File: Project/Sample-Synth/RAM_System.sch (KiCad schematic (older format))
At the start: 1 part

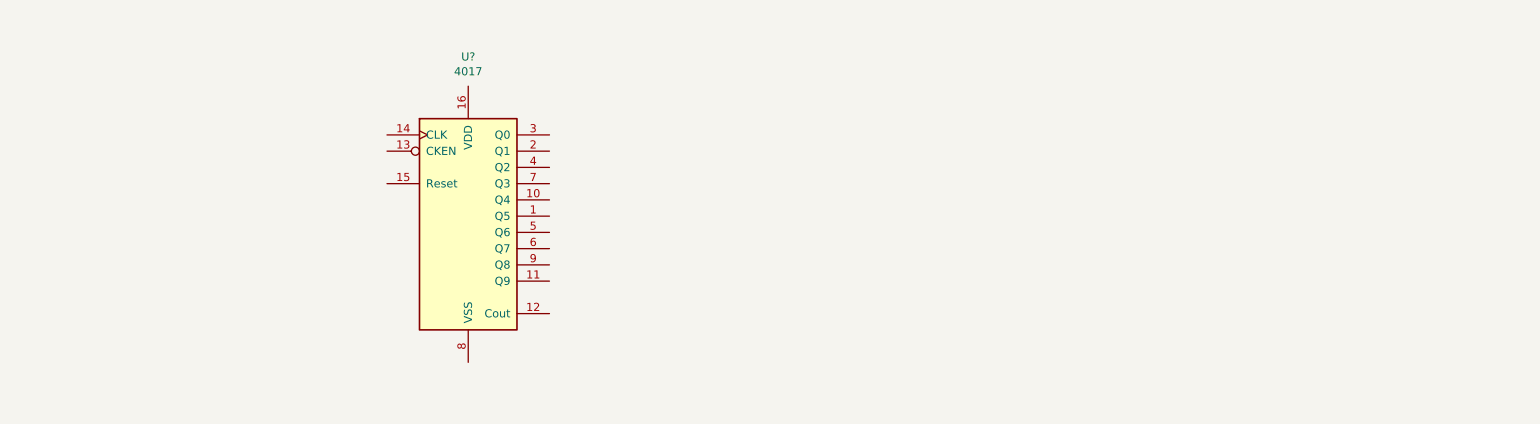
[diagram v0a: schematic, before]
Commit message: Updates to Schematic
Schematic updates: fixed connections on RAM, started setup for DAC stage.
Also swapped out the datasheet for the RAM to a more accurate one.
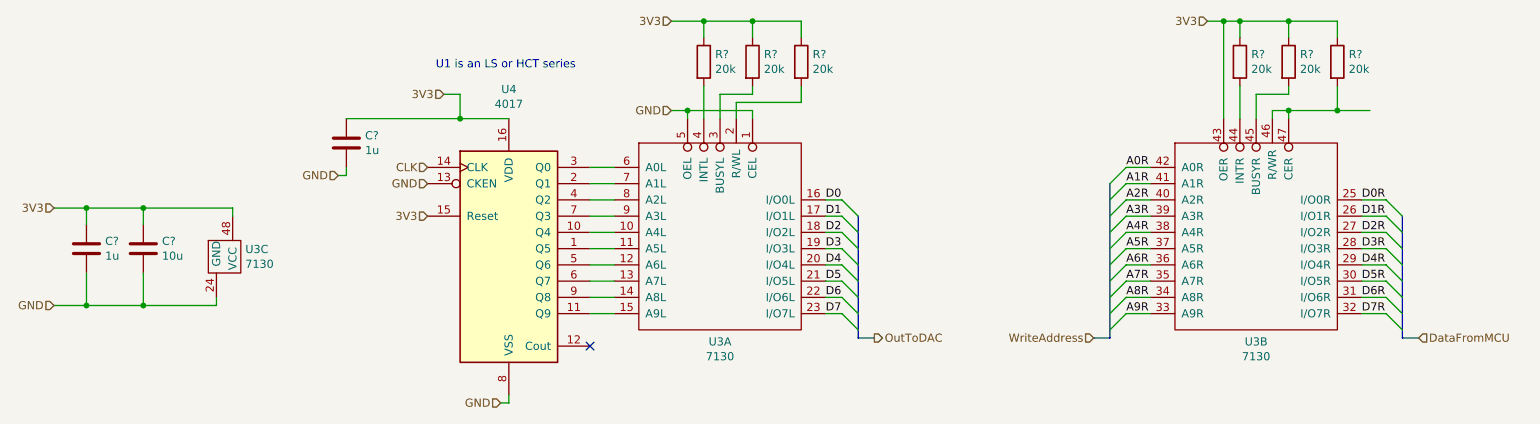
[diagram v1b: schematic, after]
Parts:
- added C? (x2): 1u, symbol Device:C
- added C?: 10u, symbol Device:C
- added R? (x6): 20k, symbol Device:R
- added U3: 7130, Package_DIP:DIP-48_W15.24mm_Socket_LongPads, symbol Memory_RAM:7130
- gave numbers to parts that had none: 1
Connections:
- net at U4.1 (Q5): now also U3.11 (A5L)
- net at U4.10 (Q4): now also U3.10 (A4L)
- net at U4.11 (Q9): now also U3.15 (A9L)
- net GND: now reaches U4.13 (CKEN)
- net GND: now also U4.8 (VSS), C?.2, C?.2, C?.2, U3.1 (CEL), U3.24 (GND), U3.5 (OEL)
- net CLK: now reaches U4.14 (CLK)
- net 3V3: now reaches U4.15 (Reset)
- net 3V3: now also U4.16 (VDD), C?.1, C?.1, C?.1, R?.1, R?.1, R?.1, R?.1, R?.1, R?.1, U3.43 (OER), U3.48 (VCC)
- net at U4.2 (Q1): now also U3.7 (A1L)
- net at U4.3 (Q0): now also U3.6 (A0L)
- net at U4.4 (Q2): now also U3.8 (A2L)
- net at U4.5 (Q6): now also U3.12 (A6L)
- net at U4.6 (Q7): now also U3.13 (A7L)
- net at U4.7 (Q3): now also U3.9 (A3L)
- net at U4.9 (Q8): now also U3.14 (A8L)
- new net: R?.2, U3.2 (R/WL)
- new net: R?.2, U3.3 (BUSYL)
- new net: R?.2, U3.4 (INTL)
- new net: R?.2, U3.44 (INTR)
- new net: R?.2, U3.45 (BUSYR)
- new net: R?.2, U3.46 (R/WR), U3.47 (CER)
- new net A0R: U3.42 (A0R)
- new net A1R: U3.41 (A1R)
- new net A2R: U3.40 (A2R)
- new net A3R: U3.39 (A3R)
- new net A4R: U3.38 (A4R)
- new net A5R: U3.37 (A5R)
- new net A6R: U3.36 (A6R)
- new net A7R: U3.35 (A7R)
- new net A8R: U3.34 (A8R)
- new net A9R: U3.33 (A9R)
- new net D0: U3.16 (I/O0L)
- new net D0R: U3.25 (I/O0R)
- new net D1: U3.17 (I/O1L)
- new net D1R: U3.26 (I/O1R)
- new net D2: U3.18 (I/O2L)
- new net D2R: U3.27 (I/O2R)
- new net D3: U3.19 (I/O3L)
- new net D3R: U3.28 (I/O3R)
- new net D4: U3.20 (I/O4L)
- new net D4R: U3.29 (I/O4R)
- new net D5: U3.21 (I/O5L)
- new net D5R: U3.30 (I/O5R)
- new net D6: U3.22 (I/O6L)
- new net D6R: U3.31 (I/O6R)
- new net D7: U3.23 (I/O7L)
- new net D7R: U3.32 (I/O7R)
- no-connect marks 0 -> 1
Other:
- note added: "U1 is an LS or HCT series"
- moved on the sheet: U4
